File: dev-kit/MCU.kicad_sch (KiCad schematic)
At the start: 38 parts, among them IC301 FAN5624UMPX, IC302 MX25U51245GZ4I00, IC303 USBLC6-2P6, IC304 NTS0104GU12, J301 Jumper, J302 Jumper, J303 Jumper, J304 Jumper, M301 NORA-B106, X301 Power, X302 Power, X303 Device, X304 GPIO, X305 UART, X306 IO Power, X307 Display, X308 Touch Power, X309 LED Power, X310 DEBUG

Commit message: Issue #117
Signed-off-by: Daniel Kampert <DanielKampert@kampis-elektroecke.de>
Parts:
- X301, X302, X306, X308, X309: footprint Connector_PinHeader_2.54mm:PinHeader_1x02_P2.54mm_Vertical_SMD_Pin1Left -> Connector_PinHeader_2.54mm:PinHeader_1x02_P2.54mm_Vertical_SMD_Pin1Right
- X304: footprint Connector_PinHeader_2.54mm:PinHeader_1x06_P2.54mm_Vertical_SMD_Pin1Left -> Connector_PinHeader_2.54mm:PinHeader_1x06_P2.54mm_Vertical_SMD_Pin1Right
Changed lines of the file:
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@@
 		(title "Watch-HW")
 		(date "2025-05-09")
-		(rev "0")
+		(rev "2")
 		(company "https://github.com/ZSWatch/Watch-HW")
 	)
@@
 			)
 		)
-		(property "Footprint" "Connector_PinHeader_2.54mm:PinHeader_1x02_P2.54mm_Vertical_SMD_Pin1Left"
+		(property "Footprint" "Connector_PinHeader_2.54mm:PinHeader_1x02_P2.54mm_Vertical_SMD_Pin1Right"
 			(at 53.34 68.58 0)
 			(effects
@@
 			)
 		)
-		(property "Footprint" "Connector_PinHeader_2.54mm:PinHeader_1x02_P2.54mm_Vertical_SMD_Pin1Left"
+		(property "Footprint" "Connector_PinHeader_2.54mm:PinHeader_1x02_P2.54mm_Vertical_SMD_Pin1Right"
 			(at 63.5 234.95 0)
 			(effects
@@
 			)
 		)
-		(property "Footprint" "Connector_PinHeader_2.54mm:PinHeader_1x02_P2.54mm_Vertical_SMD_Pin1Left"
+		(property "Footprint" "Connector_PinHeader_2.54mm:PinHeader_1x02_P2.54mm_Vertical_SMD_Pin1Right"
 			(at 363.22 114.3 0)
 			(effects
@@
 			)
 		)
-		(property "Footprint" "Connector_PinHeader_2.54mm:PinHeader_1x02_P2.54mm_Vertical_SMD_Pin1Left"
+		(property "Footprint" "Connector_PinHeader_2.54mm:PinHeader_1x02_P2.54mm_Vertical_SMD_Pin1Right"
 			(at 344.17 114.3 0)
 			(effects
@@
 			)
 		)
-		(property "Footprint" "Connector_PinHeader_2.54mm:PinHeader_1x06_P2.54mm_Vertical_SMD_Pin1Left"
+		(property "Footprint" "Connector_PinHeader_2.54mm:PinHeader_1x06_P2.54mm_Vertical_SMD_Pin1Right"
 			(at 207.01 36.83 0)
 			(effects
@@
 			)
 		)
-		(property "Footprint" "Connector_PinHeader_2.54mm:PinHeader_1x02_P2.54mm_Vertical_SMD_Pin1Left"
+		(property "Footprint" "Connector_PinHeader_2.54mm:PinHeader_1x02_P2.54mm_Vertical_SMD_Pin1Right"
 			(at 374.65 163.83 0)
 			(effects

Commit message: Feature: Issue #153
Signed-off-by: Daniel Kampert <DanielKampert@kampis-elektroecke.de>
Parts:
- X310: footprint Connector_PinHeader_1.27mm:PinHeader_2x05_P1.27mm_Vertical -> Samtec:SHF-105-01-L-D-SM-TR; manf Samtec -> Wurth Elektronik; manf# SHF-105-01-L-D-TH-TR -> 623310235521; mouser# 200-SHF-105-01-L-D-TH-TR -> 710-623310235521
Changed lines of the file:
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@@
 			)
 		)
-		(property "Footprint" "Connector_PinHeader_1.27mm:PinHeader_2x05_P1.27mm_Vertical"
+		(property "Footprint" "Samtec:SHF-105-01-L-D-SM-TR"
 			(at 382.27 227.33 0)
 			(effects
@@
 			)
 		)
-		(property "manf" "Samtec"
+		(property "manf" "Wurth Elektronik"
 			(at 382.27 227.33 0)
 			(effects
@@
 			)
 		)
-		(property "manf#" "SHF-105-01-L-D-TH-TR"
+		(property "manf#" "623310235521"
 			(at 382.27 227.33 0)
 			(effects
@@
 			)
 		)
-		(property "mouser#" "200-SHF-105-01-L-D-TH-TR"
+		(property "mouser#" "710-623310235521"
 			(at 382.27 227.33 0)
 			(effects

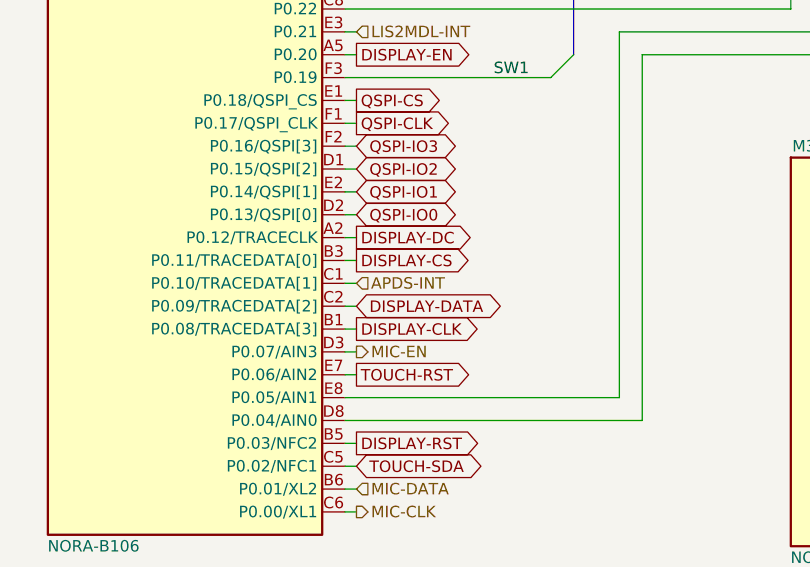
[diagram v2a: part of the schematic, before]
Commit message: Task: Issue #122
Signed-off-by: Daniel Kampert <DanielKampert@kampis-elektroecke.de>
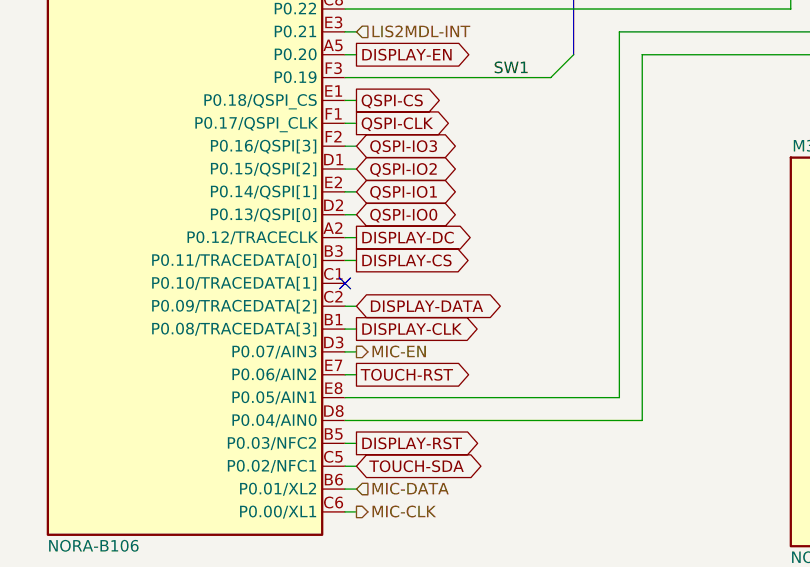
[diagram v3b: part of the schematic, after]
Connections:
- net APDS-INT: no longer names the net of M301.C1 (P0.10/TRACEDATA[1])
- no-connect marks 12 -> 13
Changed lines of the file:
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@@
 	)
 	(no_connect
+		(at 152.4 114.3)
+	)
+	(no_connect
 		(at 152.4 66.04)
 	)
@@
 	(wire
 		(pts
-			(xy 152.4 114.3) (xy 153.67 114.3)
-		)
-		(stroke
-			(width 0)
-			(type default)
-		)
-	)
-	(wire
-		(pts
 			(xy 191.77 217.17) (xy 186.69 217.17)
 		)
@@
 		(effects
 			(font
-				(size 1.27 1.27)
-			)
-			(justify left)
-		)
-	)
-	(hierarchical_label "APDS-INT"
-		(shape input)
-		(at 153.67 114.3 0)
-		(effects
-			(font

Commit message: Bug: Issue #121
Signed-off-by: Daniel Kampert <DanielKampert@kampis-elektroecke.de>
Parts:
- X301, X302, X306, X308, X309: footprint Connector_PinHeader_2.54mm:PinHeader_1x02_P2.54mm_Vertical_SMD_Pin1Right -> Connector_PinHeader_2.54mm:PinHeader_1x02_P2.54mm_Vertical; manf# 10129380-902001BLF -> 77311-818-02LF; mouser# 649-1012938090201BLF -> 649-77311-818-02LF
- X304: footprint Connector_PinHeader_2.54mm:PinHeader_1x06_P2.54mm_Vertical_SMD_Pin1Right -> Connector_PinHeader_2.54mm:PinHeader_1x06_P2.54mm_Vertical; manf# 10129380-906002ALF -> 77311-802-06LF; mouser# 649-1012938090602ALF -> 649-77311-802-06LF
- X305: manf# 10129378-936001BLF -> 77311-818-03LF; mouser# 649-1012937893601BLF -> 649-77311-818-03LF
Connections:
- net +1V8: now also X301.1 (Pin_1), X302.1 (Pin_1); no longer X301.2 (Pin_2), X302.2 (Pin_2)
- net at M301.A7 (VDD), M301.A8 (VDDH), M301.B7 (VDD): now also X301.2 (Pin_2); no longer X301.1 (Pin_1)
- net at C302.2, IC302.8 (VCC): now also X302.2 (Pin_2); no longer X302.1 (Pin_1)
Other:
- moved on the sheet: X301, X302
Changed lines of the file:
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@@
 	(symbol
 		(lib_id "Connector_Generic:Conn_01x02")
-		(at 53.34 68.58 180)
+		(at 53.34 66.04 0)
+		(mirror y)
 		(unit 1)
 		(exclude_from_sim no)
@@
 			)
 		)
-		(property "Footprint" "Connector_PinHeader_2.54mm:PinHeader_1x02_P2.54mm_Vertical_SMD_Pin1Right"
-			(at 53.34 68.58 0)
+		(property "Footprint" "Connector_PinHeader_2.54mm:PinHeader_1x02_P2.54mm_Vertical"
+			(at 53.34 66.04 0)
 			(effects
 				(font
@@
 		)
 		(property "Datasheet" "https://cdn.amphenol-cs.com/media/wysiwyg/files/documentation/datasheet/boardwiretoboard/bwb_econostik_254headers.pdf"
-			(at 53.34 68.58 0)
+			(at 53.34 66.04 0)
 			(effects
 				(font
@@
 		)
 		(property "Description" "Generic connector, single row, 01x02, script generated (kicad-library-utils/schlib/autogen/connector/)"
-			(at 53.34 68.58 0)
+			(at 53.34 66.04 0)
 			(effects
 				(font
@@
 		)
 		(property "manf" "Amphenol FCI"
-			(at 53.34 68.58 0)
+			(at 53.34 66.04 0)
 			(effects
 				(font
@@
 			)
 		)
-		(property "manf#" "10129380-902001BLF"
-			(at 53.34 68.58 0)
+		(property "manf#" "77311-818-02LF"
+			(at 53.34 66.04 0)
 			(effects
 				(font
@@
 			)
 		)
-		(property "mouser#" "649-1012938090201BLF"
-			(at 53.34 68.58 0)
+		(property "mouser#" "649-77311-818-02LF"
+			(at 53.34 66.04 0)
 			(effects
 				(font
@@
 		)
 		(property "CONFIG" ""
-			(at 53.34 68.58 0)
+			(at 53.34 66.04 0)
 			(effects
 				(font
@@
 	(symbol
 		(lib_id "Connector_Generic:Conn_01x02")
-		(at 63.5 234.95 180)
+		(at 63.5 232.41 0)
+		(mirror y)
 		(unit 1)
 		(exclude_from_sim no)
@@
 			)
 		)
-		(property "Footprint" "Connector_PinHeader_2.54mm:PinHeader_1x02_P2.54mm_Vertical_SMD_Pin1Right"
-			(at 63.5 234.95 0)
+		(property "Footprint" "Connector_PinHeader_2.54mm:PinHeader_1x02_P2.54mm_Vertical"
+			(at 63.5 232.41 0)
 			(effects
 				(font
@@
 		)
 		(property "Datasheet" "https://cdn.amphenol-cs.com/media/wysiwyg/files/documentation/datasheet/boardwiretoboard/bwb_econostik_254headers.pdf"
-			(at 63.5 234.95 0)
+			(at 63.5 232.41 0)
 			(effects
 				(font
@@
 		)
 		(property "Description" "Generic connector, single row, 01x02, script generated (kicad-library-utils/schlib/autogen/connector/)"
-			(at 63.5 234.95 0)
+			(at 63.5 232.41 0)
 			(effects
 				(font
@@
 		)
 		(property "manf" "Amphenol FCI"
-			(at 63.5 234.95 0)
+			(at 63.5 232.41 0)
 			(effects
 				(font
@@
 			)
 		)
-		(property "manf#" "10129380-902001BLF"
-			(at 63.5 234.95 0)
+		(property "manf#" "77311-818-02LF"
+			(at 63.5 232.41 0)
 			(effects
 				(font
@@
 			)
 		)
-		(property "mouser#" "649-1012938090201BLF"
-			(at 63.5 234.95 0)
+		(property "mouser#" "649-77311-818-02LF"
+			(at 63.5 232.41 0)
 			(effects
 				(font
@@
 		)
 		(property "CONFIG" ""
-			(at 63.5 234.95 0)
+			(at 63.5 232.41 0)
 			(effects
 				(font
@@
 			)
 		)
-		(property "manf#" "10129378-936001BLF"
+		(property "manf#" "77311-818-03LF"
 			(at 218.44 274.32 0)
 			(effects
@@
 			)
 		)
-		(property "mouser#" "649-1012937893601BLF"
+		(property "mouser#" "649-77311-818-03LF"
 			(at 218.44 274.32 0)
 			(effects
@@
 			)
 		)
-		(property "Footprint" "Connector_PinHeader_2.54mm:PinHeader_1x02_P2.54mm_Vertical_SMD_Pin1Right"
+		(property "Footprint" "Connector_PinHeader_2.54mm:PinHeader_1x02_P2.54mm_Vertical"
 			(at 363.22 114.3 0)
 			(effects
@@
 			)
 		)
-		(property "manf#" "10129380-902001BLF"
+		(property "manf#" "77311-818-02LF"
 			(at 363.22 114.3 0)
 			(effects
@@
 			)
 		)
-		(property "mouser#" "649-1012938090201BLF"
+		(property "mouser#" "649-77311-818-02LF"
 			(at 363.22 114.3 0)
 			(effects
@@
 			)
 		)
-		(property "Footprint" "Connector_PinHeader_2.54mm:PinHeader_1x02_P2.54mm_Vertical_SMD_Pin1Right"
+		(property "Footprint" "Connector_PinHeader_2.54mm:PinHeader_1x02_P2.54mm_Vertical"
 			(at 344.17 114.3 0)
 			(effects
@@
 			)
 		)
-		(property "manf#" "10129380-902001BLF"
+		(property "manf#" "77311-818-02LF"
 			(at 344.17 114.3 0)
 			(effects
@@
 			)
 		)
-		(property "mouser#" "649-1012938090201BLF"
+		(property "mouser#" "649-77311-818-02LF"
 			(at 344.17 114.3 0)
 			(effects
@@
 			)
 		)
-		(property "Footprint" "Connector_PinHeader_2.54mm:PinHeader_1x06_P2.54mm_Vertical_SMD_Pin1Right"
+		(property "Footprint" "Connector_PinHeader_2.54mm:PinHeader_1x06_P2.54mm_Vertical"
 			(at 207.01 36.83 0)
 			(effects
@@
 			)
 		)
-		(property "manf#" "10129380-906002ALF"
+		(property "manf#" "77311-802-06LF"
 			(at 207.01 36.83 0)
 			(effects
@@
 			)
 		)
-		(property "mouser#" "649-1012938090602ALF"
+		(property "mouser#" "649-77311-802-06LF"
 			(at 207.01 36.83 0)
 			(effects
@@
 			)
 		)
-		(property "Footprint" "Connector_PinHeader_2.54mm:PinHeader_1x02_P2.54mm_Vertical_SMD_Pin1Right"
+		(property "Footprint" "Connector_PinHeader_2.54mm:PinHeader_1x02_P2.54mm_Vertical"
 			(at 374.65 163.83 0)
 			(effects
@@
 			)
 		)
-		(property "manf#" "10129380-902001BLF"
+		(property "manf#" "77311-818-02LF"
 			(at 374.65 163.83 0)
 			(effects
@@
 			)
 		)
-		(property "mouser#" "649-1012938090201BLF"
+		(property "mouser#" "649-77311-818-02LF"
 			(at 374.65 163.83 0)
 			(effects

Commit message: Task: Issue #123
Signed-off-by: Daniel Kampert <DanielKampert@kampis-elektroecke.de>
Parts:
- added R315, R316: 100k, Resistor_SMD:R_0805_2012Metric, symbol Device:R_Small
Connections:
- net +1V8: now also R315.2
- net DISPLAY-EN: now also R315.1, R316.2
- net GND: now also R316.1
